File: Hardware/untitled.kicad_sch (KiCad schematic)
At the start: 5 parts, among them J2 Conn_Coaxial

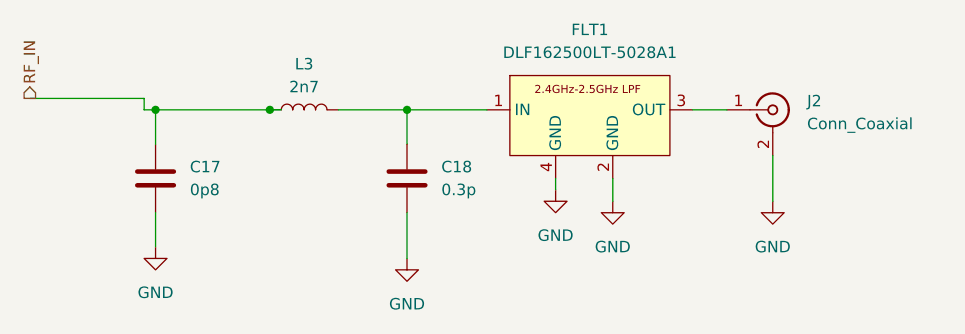
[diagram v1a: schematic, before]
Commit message: [Hierachisation] hierachisation de la schématique et ajout de l'USB
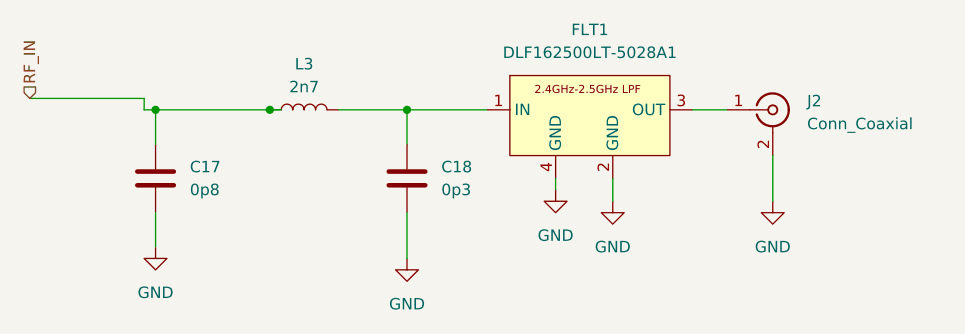
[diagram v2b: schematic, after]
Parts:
- C18: value 0.3p -> 0p3
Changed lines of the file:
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@@
 	)
 	(hierarchical_label "RF_IN"
-		(shape output)
+		(shape input)
 		(at 67.31 62.23 90)
 		(effects
@@
 			)
 		)
-		(property "Value" "0.3p"
+		(property "Value" "0p3"
 			(at 113.03 72.3899 0)
 			(effects

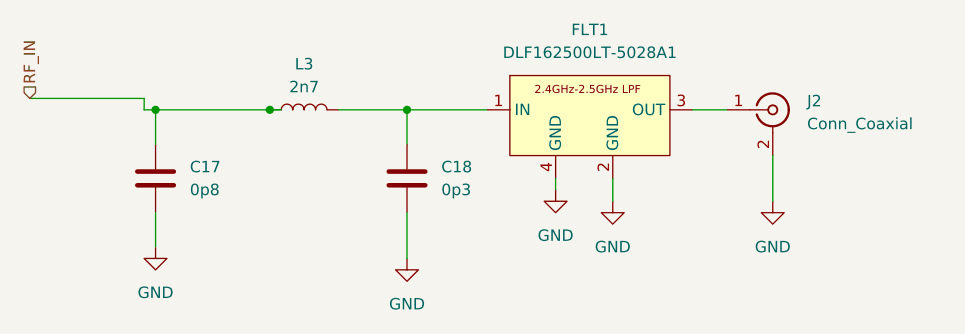
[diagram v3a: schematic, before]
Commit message: [Realisation] : Regulateur de Tension, Capteur BME280, Buzzer, MQ2 et Leds indicateurs.
Dans cette phase, j'ai réalisé les montages suivantes ;
Regulateur de Tension : La tension d'alimentation du système vient de
l'USB, donc en utilisant un regulateur de tension, on parvient à
abaisser la tension à 3.3V
Capteur BME280 : Le montage est réalisé comme recommandé par le
fabricant Bosch. En y précisant les résistance pull up pour le protocol
I2C.
Buzzer : Le buzzer va servir d'alerte en raisonnant.
Pour ce montage on utilise un transistor NPN pour amplifier le courant.
MQ2 : Pour ce capteur, on utilise des éléments traversant et de ce fait,
on va juste souder le composant à la carte.
Led Indicateurs : ces indicateurs vont servir de visuel pour juger le
niveau de la temperature.
D1 : Pour indiquer que la carte est sous tension
D2 : Pour indiquer que la temperature est < 20°C
D3 : Pour indiquer que la temperature est > 20°C et < 30°C
D4 : Pour indiquer que la temperature est > 30°C
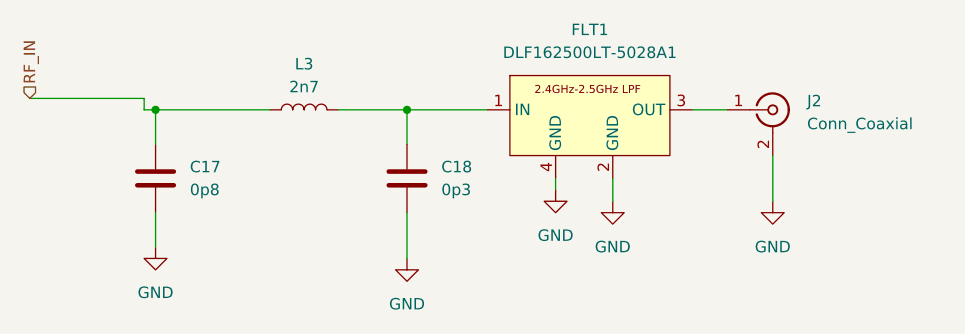
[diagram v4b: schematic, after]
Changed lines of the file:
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@@
-		(color 0 0 0 0)
-	)
-	(junction
-		(at 93.98 63.5)
-		(diameter 0)
 		(color 0 0 0 0)
 	)
@@
 		(pts
 			(xy 67.31 62.23) (xy 80.01 62.23)
-		)
-		(stroke
-			(width 0)
-			(type default)
-		)
-	)
-	(wire
-		(pts
-			(xy 81.28 63.5) (xy 93.98 63.5)
 		)
 		(stroke
@@
 	(wire
 		(pts
+			(xy 81.28 63.5) (xy 93.98 63.5)
+		)
+		(stroke
+			(width 0)
+			(type default)
+		)
+	)
+	(wire
+		(pts
 			(xy 80.01 62.23) (xy 80.01 63.5)
 		)
@@
 		)
 		(stroke
-			(width 0)
-			(type default)
-		)
-	)
-	(wire
-		(pts
-			(xy 93.98 63.5) (xy 95.25 63.5)
-		)
-		(stroke
